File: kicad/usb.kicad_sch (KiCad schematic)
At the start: 4 parts, among them J7 USB_C_Receptacle_USB2.0_14P, U15 USBLC6-2SC6

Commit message: checking shunt footprints
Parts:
- renumbered J7 to J9, R37 to R45, R36 to R46
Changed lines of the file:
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@@
 		(on_board yes)
 		(dnp no)
-		(property "Reference" "R37"
+		(property "Reference" "R45"
 			(at 119.888 76.2 90)
 			(effects
@@
 			(project "resc"
 				(path "/83aea3b7-5b9b-498e-8d41-e84fae2f87fa/5f81bd15-f3fb-48c3-8997-18d2496b9ffc"
-					(reference "R37")
+					(reference "R45")
 					(unit 1)
 				)
@@
 		(dnp no)
 		(fields_autoplaced yes)
-		(property "Reference" "#PWR078"
+		(property "Reference" "#PWR089"
 			(at 92.71 120.65 0)
 			(effects
@@
 			(project "resc"
 				(path "/83aea3b7-5b9b-498e-8d41-e84fae2f87fa/5f81bd15-f3fb-48c3-8997-18d2496b9ffc"
-					(reference "#PWR078")
+					(reference "#PWR089")
 					(unit 1)
 				)
@@
 		(dnp no)
 		(fields_autoplaced yes)
-		(property "Reference" "#PWR082"
+		(property "Reference" "#PWR090"
 			(at 129.54 123.19 0)
 			(effects
@@
 			(project "resc"
 				(path "/83aea3b7-5b9b-498e-8d41-e84fae2f87fa/5f81bd15-f3fb-48c3-8997-18d2496b9ffc"
-					(reference "#PWR082")
+					(reference "#PWR090")
 					(unit 1)
 				)
@@
 		(on_board yes)
 		(dnp no)
-		(property "Reference" "#PWR080"
+		(property "Reference" "#PWR088"
 			(at 129.54 101.6 0)
 			(effects
@@
 			(project "resc"
 				(path "/83aea3b7-5b9b-498e-8d41-e84fae2f87fa/5f81bd15-f3fb-48c3-8997-18d2496b9ffc"
-					(reference "#PWR080")
+					(reference "#PWR088")
 					(unit 1)
 				)
@@
 		(dnp no)
 		(fields_autoplaced yes)
-		(property "Reference" "#PWR079"
+		(property "Reference" "#PWR086"
 			(at 114.3 73.66 0)
 			(effects
@@
 			(project ""
 				(path "/83aea3b7-5b9b-498e-8d41-e84fae2f87fa/5f81bd15-f3fb-48c3-8997-18d2496b9ffc"
-					(reference "#PWR079")
+					(reference "#PWR086")
 					(unit 1)
 				)
@@
 		(on_board yes)
 		(dnp no)
-		(property "Reference" "R36"
+		(property "Reference" "R46"
 			(at 119.634 81.28 90)
 			(effects
@@
 			(project "resc"
 				(path "/83aea3b7-5b9b-498e-8d41-e84fae2f87fa/5f81bd15-f3fb-48c3-8997-18d2496b9ffc"
-					(reference "R36")
+					(reference "R46")
 					(unit 1)
 				)
@@
 		(dnp no)
 		(fields_autoplaced yes)
-		(property "Reference" "J7"
+		(property "Reference" "J9"
 			(at 92.71 64.77 0)
 			(effects
@@
 			(project "resc"
 				(path "/83aea3b7-5b9b-498e-8d41-e84fae2f87fa/5f81bd15-f3fb-48c3-8997-18d2496b9ffc"
-					(reference "J7")
+					(reference "J9")
 					(unit 1)
 				)
@@
 		(on_board yes)
 		(dnp no)
-		(property "Reference" "#PWR081"
+		(property "Reference" "#PWR087"
 			(at 138.43 87.63 0)
 			(effects
@@
 			(project "resc"
 				(path "/83aea3b7-5b9b-498e-8d41-e84fae2f87fa/5f81bd15-f3fb-48c3-8997-18d2496b9ffc"
-					(reference "#PWR081")
-					(unit 1)
-				)
+					(reference "#PWR087")
+					(unit 1)
+				)

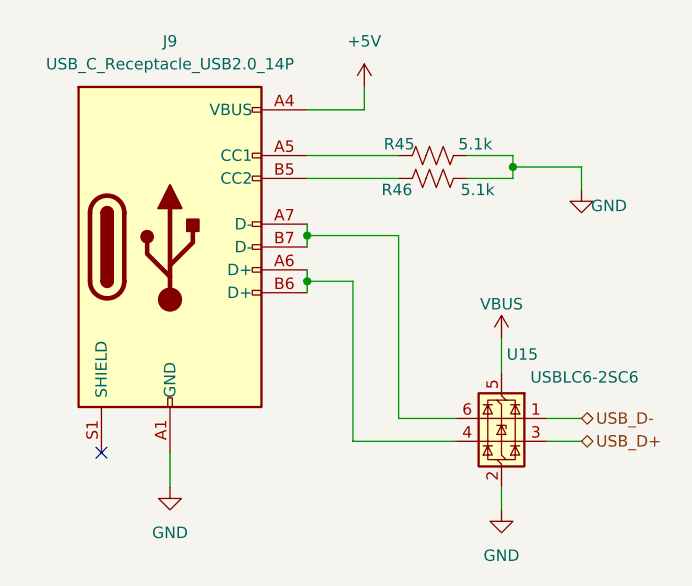
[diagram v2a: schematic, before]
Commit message: gate driver routed to mosfets, working on misc stm32 related components
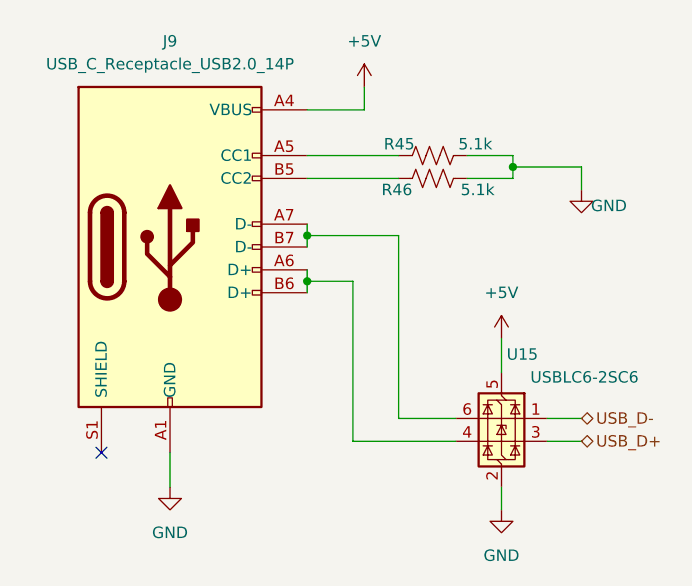
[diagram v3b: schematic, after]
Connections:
- net VBUS is gone; now on net +5V: U15.5 (VBUS)
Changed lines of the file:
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@@
 	)
 	(symbol
-		(lib_id "power:VBUS")
+		(lib_id "power:+5V")
 		(at 129.54 97.79 0)
 		(unit 1)
@@
 		(on_board yes)
 		(dnp no)
-		(property "Reference" "#PWR088"
+		(fields_autoplaced yes)
+		(property "Reference" "#PWR026"
 			(at 129.54 101.6 0)
 			(effects
@@
 			)
 		)
-		(property "Value" "VBUS"
-			(at 129.54 93.98 0)
+		(property "Value" "+5V"
+			(at 129.54 92.71 0)
 			(effects
 				(font
@@
 			)
 		)
-		(property "Description" "Power symbol creates a global label with name \"VBUS\""
+		(property "Description" "Power symbol creates a global label with name \"+5V\""
 			(at 129.54 97.79 0)
 			(effects
@@
 		)
 		(instances
-			(project "resc"
+			(project ""
 				(path "/83aea3b7-5b9b-498e-8d41-e84fae2f87fa/5f81bd15-f3fb-48c3-8997-18d2496b9ffc"
-					(reference "#PWR088")
+					(reference "#PWR026")
 					(unit 1)
 				)

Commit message: finalizing schematic for gate driver
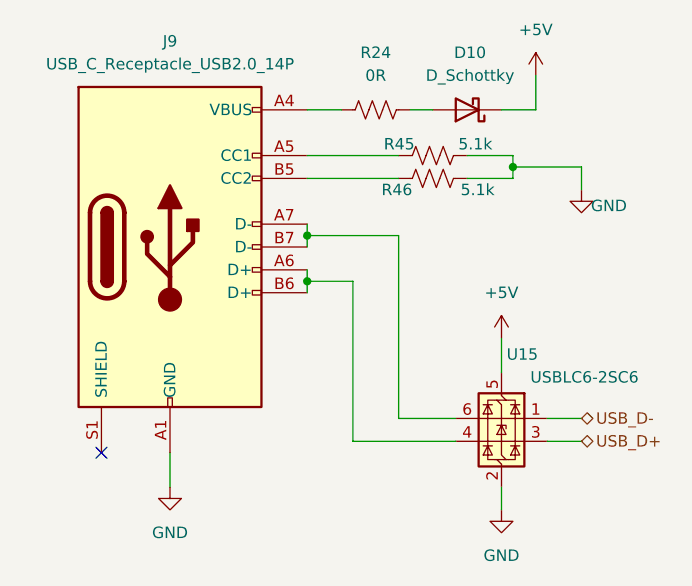
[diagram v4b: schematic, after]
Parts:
- added D10: D_Schottky, Diode_SMD:D_SOD-323_HandSoldering, symbol Device:D_Schottky
- added R24: 0R, Resistor_SMD:R_0402_1005Metric, symbol Device:R_US
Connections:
- net +5V: now also D10.1 (K); no longer J9.A4 (VBUS), J9.A9 (VBUS), J9.B4 (VBUS), J9.B9 (VBUS)
- new net: D10.2 (A), R24.2
- new net: J9.A4 (VBUS), J9.A9 (VBUS), J9.B4 (VBUS), J9.B9 (VBUS), R24.1
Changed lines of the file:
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@@
+	(wire
+		(pts
+			(xy 119.38 72.39) (xy 121.92 72.39)
+		)
+		(stroke
+			(width 0)
+			(type default)
+		)
+	)
 	(wire
 		(pts
@@
 	(wire
 		(pts
-			(xy 114.3 72.39) (xy 114.3 69.85)
+			(xy 133.35 72.39) (xy 133.35 68.58)
 		)
 		(stroke
@@
 	(wire
 		(pts
+			(xy 129.54 72.39) (xy 133.35 72.39)
+		)
+		(stroke
+			(width 0)
+			(type default)
+		)
+	)
+	(wire
+		(pts
 			(xy 129.54 114.3) (xy 129.54 116.84)
 		)
@@
 	(wire
 		(pts
+			(xy 107.95 72.39) (xy 111.76 72.39)
+		)
+		(stroke
+			(width 0)
+			(type default)
+		)
+	)
+	(wire
+		(pts
 			(xy 107.95 77.47) (xy 118.11 77.47)
-		)
-		(stroke
-			(width 0)
-			(type default)
-		)
-	)
-	(wire
-		(pts
-			(xy 107.95 72.39) (xy 114.3 72.39)
 		)
 		(stroke
@@
 	(symbol
 		(lib_id "power:+5V")
-		(at 114.3 69.85 0)
+		(at 133.35 68.58 0)
 		(unit 1)
 		(exclude_from_sim no)
@@
 		(fields_autoplaced yes)
 		(property "Reference" "#PWR086"
-			(at 114.3 73.66 0)
+			(at 133.35 72.39 0)
 			(effects
 				(font
@@
 		)
 		(property "Value" "+5V"
-			(at 114.3 64.77 0)
+			(at 133.35 63.5 0)
 			(effects
 				(font
@@
 		)
 		(property "Footprint" ""
-			(at 114.3 69.85 0)
+			(at 133.35 68.58 0)
 			(effects
 				(font
@@
 		)
 		(property "Datasheet" ""
-			(at 114.3 69.85 0)
+			(at 133.35 68.58 0)
 			(effects
 				(font
@@
 		)
 		(property "Description" "Power symbol creates a global label with name \"+5V\""
-			(at 114.3 69.85 0)
+			(at 133.35 68.58 0)
 			(effects
 				(font
@@
 				(path "/83aea3b7-5b9b-498e-8d41-e84fae2f87fa/5f81bd15-f3fb-48c3-8997-18d2496b9ffc"
 					(reference "#PWR086")
+					(unit 1)
+				)
+			)
+		)
+	)
+	(symbol
+		(lib_id "Device:D_Schottky")
+		(at 125.73 72.39 180)
+		(unit 1)
+		(exclude_from_sim no)
+		(in_bom yes)
+		(on_board yes)
+		(dnp no)
+		(fields_autoplaced yes)
+		(property "Reference" "D10"
+			(at 126.0475 66.04 0)
+			(effects
+				(font
+					(size 1.27 1.27)
+				)
+			)
+		)
+		(property "Value" "D_Schottky"
+			(at 126.0475 68.58 0)
+			(effects
+				(font
+					(size 1.27 1.27)
+				)
+			)
+		)
+		(property "Footprint" "Diode_SMD:D_SOD-323_HandSoldering"
+			(at 125.73 72.39 0)
+			(effects
+				(font
+					(size 1.27 1.27)
+				)
+				(hide yes)
+			)
+		)
+		(property "Datasheet" "~"
+			(at 125.73 72.39 0)
+			(effects
+				(font
+					(size 1.27 1.27)
+				)
+				(hide yes)
+			)
+		)
+		(property "Description" "Schottky diode"
+			(at 125.73 72.39 0)
+			(effects
+				(font
+					(size 1.27 1.27)
+				)
+				(hide yes)
+			)
+		)
+		(pin "1"
+		)
+		(pin "2"
+		)
+		(instances
+			(project ""
+				(path "/83aea3b7-5b9b-498e-8d41-e84fae2f87fa/5f81bd15-f3fb-48c3-8997-18d2496b9ffc"
+					(reference "D10")
 					(unit 1)
 				)
@@
 					(unit 1)
 				)
+			)
+		)
+	)
+	(symbol
+		(lib_id "Device:R_US")
+		(at 115.57 72.39 90)
+		(unit 1)
+		(exclude_from_sim no)
+		(in_bom yes)
+		(on_board yes)
+		(dnp no)
+		(fields_autoplaced yes)
+		(property "Reference" "R24"
+			(at 115.57 66.04 90)
+			(effects
+				(font
+					(size 1.27 1.27)
+				)
+			)
+		)
+		(property "Value" "0R"
+			(at 115.57 68.58 90)
+			(effects
+				(font
+					(size 1.27 1.27)
+				)
+			)
+		)
+		(property "Footprint" "Resistor_SMD:R_0402_1005Metric"
+			(at 115.824 71.374 90)
+			(effects
+				(font
+					(size 1.27 1.27)
+				)
+				(hide yes)
+			)
+		)
+		(property "Datasheet" "~"
+			(at 115.57 72.39 0)
+			(effects
+				(font
+					(size 1.27 1.27)
+				)
+				(hide yes)
+			)
+		)
+		(property "Description" "Resistor, US symbol"
+			(at 115.57 72.39 0)
+			(effects
+				(font
+					(size 1.27 1.27)
+				)
+				(hide yes)
+			)
+		)
+		(pin "2"
+		)
+		(pin "1"
+		)
+		(instances
+			(project ""
+				(path "/83aea3b7-5b9b-498e-8d41-e84fae2f87fa/5f81bd15-f3fb-48c3-8997-18d2496b9ffc"
+					(reference "R24")
+					(unit 1)
+				)

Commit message: revert to v6.05
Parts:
- removed R24: 0R, Resistor_SMD:R_0402_1005Metric, symbol Device:R_US
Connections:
- net at D10.2 (A): now also J9.A4 (VBUS), J9.A9 (VBUS), J9.B4 (VBUS), J9.B9 (VBUS)
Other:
- moved on the sheet: D10
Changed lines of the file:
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@@
-	(wire
-		(pts
-			(xy 119.38 72.39) (xy 121.92 72.39)
-		)
-		(stroke
-			(width 0)
-			(type default)
-		)
-	)
 	(wire
 		(pts
@@
 	(wire
 		(pts
+			(xy 123.19 72.39) (xy 133.35 72.39)
+		)
+		(stroke
+			(width 0)
+			(type default)
+		)
+	)
+	(wire
+		(pts
 			(xy 133.35 72.39) (xy 133.35 68.58)
 		)
@@
 	(wire
 		(pts
-			(xy 129.54 72.39) (xy 133.35 72.39)
-		)
-		(stroke
-			(width 0)
-			(type default)
-		)
-	)
-	(wire
-		(pts
 			(xy 129.54 114.3) (xy 129.54 116.84)
 		)
@@
 	(wire
 		(pts
+			(xy 107.95 72.39) (xy 115.57 72.39)
+		)
+		(stroke
+			(width 0)
+			(type default)
+		)
+	)
+	(wire
+		(pts
 			(xy 92.71 110.49) (xy 92.71 114.3)
 		)
@@
 		(pts
 			(xy 107.95 86.36) (xy 107.95 87.63)
-		)
-		(stroke
-			(width 0)
-			(type default)
-		)
-	)
-	(wire
-		(pts
-			(xy 107.95 72.39) (xy 111.76 72.39)
 		)
 		(stroke
@@
 	(symbol
 		(lib_id "Device:D_Schottky")
-		(at 125.73 72.39 180)
+		(at 119.38 72.39 180)
 		(unit 1)
 		(exclude_from_sim no)
@@
 		(fields_autoplaced yes)
 		(property "Reference" "D10"
-			(at 126.0475 66.04 0)
+			(at 119.6975 66.04 0)
 			(effects
 				(font
@@
 		)
 		(property "Value" "D_Schottky"
-			(at 126.0475 68.58 0)
+			(at 119.6975 68.58 0)
 			(effects
 				(font
@@
 		)
 		(property "Footprint" "Diode_SMD:D_SOD-323_HandSoldering"
-			(at 125.73 72.39 0)
+			(at 119.38 72.39 0)
 			(effects
 				(font
@@
 		)
 		(property "Datasheet" "~"
-			(at 125.73 72.39 0)
+			(at 119.38 72.39 0)
 			(effects
 				(font
@@
 		)
 		(property "Description" "Schottky diode"
-			(at 125.73 72.39 0)
+			(at 119.38 72.39 0)
 			(effects
 				(font
@@
 					(unit 1)
 				)
-			)
-		)
-	)
-	(symbol
-		(lib_id "Device:R_US")
-		(at 115.57 72.39 90)
-		(unit 1)
-		(exclude_from_sim no)
-		(in_bom yes)
-		(on_board yes)
-		(dnp no)
-		(fields_autoplaced yes)
-		(property "Reference" "R24"
-			(at 115.57 66.04 90)
-			(effects
-				(font
-					(size 1.27 1.27)
-				)
-			)
-		)
-		(property "Value" "0R"
-			(at 115.57 68.58 90)
-			(effects
-				(font
-					(size 1.27 1.27)
-				)
-			)
-		)
-		(property "Footprint" "Resistor_SMD:R_0402_1005Metric"
-			(at 115.824 71.374 90)
-			(effects
-				(font
-					(size 1.27 1.27)
-				)
-				(hide yes)
-			)
-		)
-		(property "Datasheet" "~"
-			(at 115.57 72.39 0)
-			(effects
-				(font
-					(size 1.27 1.27)
-				)
-				(hide yes)
-			)
-		)
-		(property "Description" "Resistor, US symbol"
-			(at 115.57 72.39 0)
-			(effects
-				(font
-					(size 1.27 1.27)
-				)
-				(hide yes)
-			)
-		)
-		(pin "2"
-		)
-		(pin "1"
-		)
-		(instances
-			(project ""
-				(path "/83aea3b7-5b9b-498e-8d41-e84fae2f87fa/5f81bd15-f3fb-48c3-8997-18d2496b9ffc"
-					(reference "R24")
-					(unit 1)
-				)

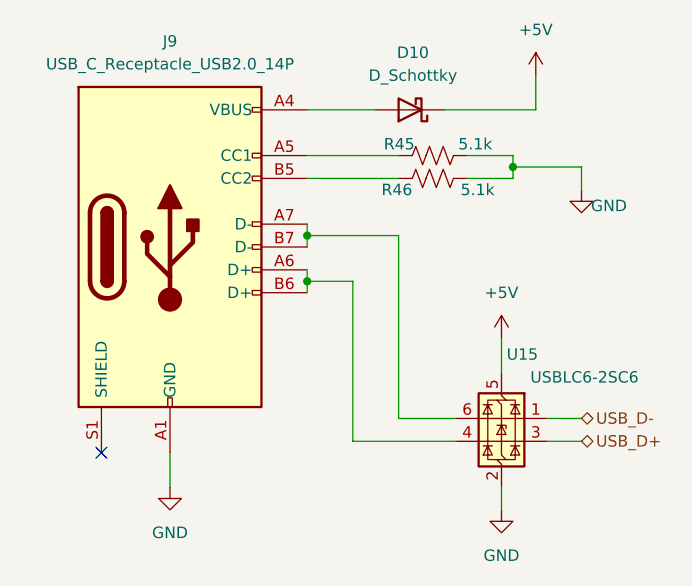
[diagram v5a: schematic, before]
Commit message: gate driver mostly schematic'd and pcb started
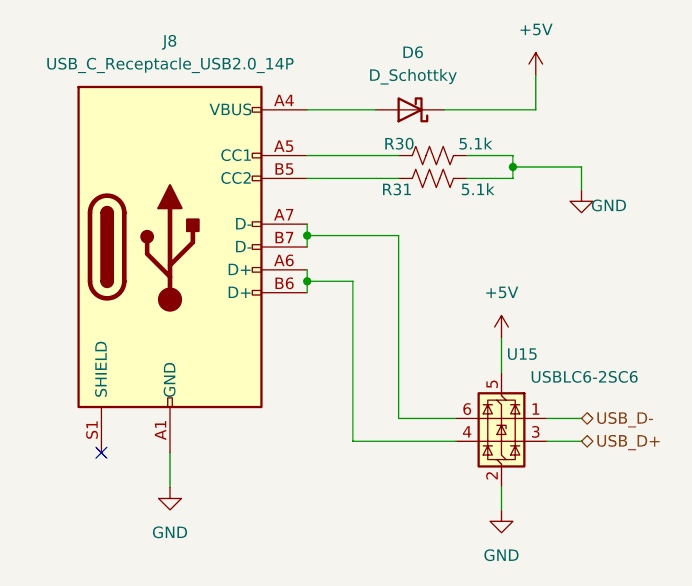
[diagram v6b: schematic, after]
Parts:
- renumbered D10 to D6, J9 to J8, R45 to R30, R46 to R31
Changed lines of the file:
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@@
 		(on_board yes)
 		(dnp no)
-		(property "Reference" "R45"
+		(property "Reference" "R30"
 			(at 119.888 76.2 90)
 			(effects
@@
 			(project "resc"
 				(path "/83aea3b7-5b9b-498e-8d41-e84fae2f87fa/5f81bd15-f3fb-48c3-8997-18d2496b9ffc"
-					(reference "R45")
+					(reference "R30")
 					(unit 1)
 				)
@@
 		(dnp no)
 		(fields_autoplaced yes)
-		(property "Reference" "#PWR089"
+		(property "Reference" "#PWR076"
 			(at 92.71 120.65 0)
 			(effects
@@
 			(project "resc"
 				(path "/83aea3b7-5b9b-498e-8d41-e84fae2f87fa/5f81bd15-f3fb-48c3-8997-18d2496b9ffc"
-					(reference "#PWR089")
+					(reference "#PWR076")
 					(unit 1)
 				)
@@
 		(dnp no)
 		(fields_autoplaced yes)
-		(property "Reference" "#PWR090"
+		(property "Reference" "#PWR077"
 			(at 129.54 123.19 0)
 			(effects
@@
 			(project "resc"
 				(path "/83aea3b7-5b9b-498e-8d41-e84fae2f87fa/5f81bd15-f3fb-48c3-8997-18d2496b9ffc"
-					(reference "#PWR090")
+					(reference "#PWR077")
 					(unit 1)
 				)
@@
 		(dnp no)
 		(fields_autoplaced yes)
-		(property "Reference" "#PWR026"
+		(property "Reference" "#PWR075"
 			(at 129.54 101.6 0)
 			(effects
@@
 			(project ""
 				(path "/83aea3b7-5b9b-498e-8d41-e84fae2f87fa/5f81bd15-f3fb-48c3-8997-18d2496b9ffc"
-					(reference "#PWR026")
+					(reference "#PWR075")
 					(unit 1)
 				)
@@
 		(dnp no)
 		(fields_autoplaced yes)
-		(property "Reference" "#PWR086"
+		(property "Reference" "#PWR073"
 			(at 133.35 72.39 0)
 			(effects
@@
 			(project ""
 				(path "/83aea3b7-5b9b-498e-8d41-e84fae2f87fa/5f81bd15-f3fb-48c3-8997-18d2496b9ffc"
-					(reference "#PWR086")
+					(reference "#PWR073")
 					(unit 1)
 				)
@@
 		(dnp no)
 		(fields_autoplaced yes)
-		(property "Reference" "D10"
+		(property "Reference" "D6"
 			(at 119.6975 66.04 0)
 			(effects
@@
 			(project ""
 				(path "/83aea3b7-5b9b-498e-8d41-e84fae2f87fa/5f81bd15-f3fb-48c3-8997-18d2496b9ffc"
-					(reference "D10")
+					(reference "D6")
 					(unit 1)
 				)
@@
 		(on_board yes)
 		(dnp no)
-		(property "Reference" "R46"
+		(property "Reference" "R31"
 			(at 119.634 81.28 90)
 			(effects
@@
 			(project "resc"
 				(path "/83aea3b7-5b9b-498e-8d41-e84fae2f87fa/5f81bd15-f3fb-48c3-8997-18d2496b9ffc"
-					(reference "R46")
+					(reference "R31")
 					(unit 1)
 				)
@@
 		(dnp no)
 		(fields_autoplaced yes)
-		(property "Reference" "J9"
+		(property "Reference" "J8"
 			(at 92.71 64.77 0)
 			(effects
@@
 			(project "resc"
 				(path "/83aea3b7-5b9b-498e-8d41-e84fae2f87fa/5f81bd15-f3fb-48c3-8997-18d2496b9ffc"
-					(reference "J9")
+					(reference "J8")
 					(unit 1)
 				)
@@
 		(on_board yes)
 		(dnp no)
-		(property "Reference" "#PWR087"
+		(property "Reference" "#PWR074"
 			(at 138.43 87.63 0)
 			(effects
@@
 			(project "resc"
 				(path "/83aea3b7-5b9b-498e-8d41-e84fae2f87fa/5f81bd15-f3fb-48c3-8997-18d2496b9ffc"
-					(reference "#PWR087")
-					(unit 1)
-				)
+					(reference "#PWR074")
+					(unit 1)
+				)

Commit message: rev3 ordered
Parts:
- renumbered D6 to D10, J8 to J9, R30 to R45, R31 to R46
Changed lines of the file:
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@@
 		(on_board yes)
 		(dnp no)
-		(property "Reference" "R30"
+		(property "Reference" "R45"
 			(at 119.888 76.2 90)
 			(effects
@@
 			(project "resc"
 				(path "/83aea3b7-5b9b-498e-8d41-e84fae2f87fa/5f81bd15-f3fb-48c3-8997-18d2496b9ffc"
-					(reference "R30")
+					(reference "R45")
 					(unit 1)
 				)
@@
 		(dnp no)
 		(fields_autoplaced yes)
-		(property "Reference" "#PWR076"
+		(property "Reference" "#PWR089"
 			(at 92.71 120.65 0)
 			(effects
@@
 			(project "resc"
 				(path "/83aea3b7-5b9b-498e-8d41-e84fae2f87fa/5f81bd15-f3fb-48c3-8997-18d2496b9ffc"
-					(reference "#PWR076")
+					(reference "#PWR089")
 					(unit 1)
 				)
@@
 		(dnp no)
 		(fields_autoplaced yes)
-		(property "Reference" "#PWR077"
+		(property "Reference" "#PWR090"
 			(at 129.54 123.19 0)
 			(effects
@@
 			(project "resc"
 				(path "/83aea3b7-5b9b-498e-8d41-e84fae2f87fa/5f81bd15-f3fb-48c3-8997-18d2496b9ffc"
-					(reference "#PWR077")
+					(reference "#PWR090")
 					(unit 1)
 				)
@@
 		(dnp no)
 		(fields_autoplaced yes)
-		(property "Reference" "#PWR075"
+		(property "Reference" "#PWR026"
 			(at 129.54 101.6 0)
 			(effects
@@
 			(project ""
 				(path "/83aea3b7-5b9b-498e-8d41-e84fae2f87fa/5f81bd15-f3fb-48c3-8997-18d2496b9ffc"
-					(reference "#PWR075")
+					(reference "#PWR026")
 					(unit 1)
 				)
@@
 		(dnp no)
 		(fields_autoplaced yes)
-		(property "Reference" "#PWR073"
+		(property "Reference" "#PWR086"
 			(at 133.35 72.39 0)
 			(effects
@@
 			(project ""
 				(path "/83aea3b7-5b9b-498e-8d41-e84fae2f87fa/5f81bd15-f3fb-48c3-8997-18d2496b9ffc"
-					(reference "#PWR073")
+					(reference "#PWR086")
 					(unit 1)
 				)
@@
 		(dnp no)
 		(fields_autoplaced yes)
-		(property "Reference" "D6"
+		(property "Reference" "D10"
 			(at 119.6975 66.04 0)
 			(effects
@@
 			(project ""
 				(path "/83aea3b7-5b9b-498e-8d41-e84fae2f87fa/5f81bd15-f3fb-48c3-8997-18d2496b9ffc"
-					(reference "D6")
+					(reference "D10")
 					(unit 1)
 				)
@@
 		(on_board yes)
 		(dnp no)
-		(property "Reference" "R31"
+		(property "Reference" "R46"
 			(at 119.634 81.28 90)
 			(effects
@@
 			(project "resc"
 				(path "/83aea3b7-5b9b-498e-8d41-e84fae2f87fa/5f81bd15-f3fb-48c3-8997-18d2496b9ffc"
-					(reference "R31")
+					(reference "R46")
 					(unit 1)
 				)
@@
 		(dnp no)
 		(fields_autoplaced yes)
-		(property "Reference" "J8"
+		(property "Reference" "J9"
 			(at 92.71 64.77 0)
 			(effects
@@
 			(project "resc"
 				(path "/83aea3b7-5b9b-498e-8d41-e84fae2f87fa/5f81bd15-f3fb-48c3-8997-18d2496b9ffc"
-					(reference "J8")
+					(reference "J9")
 					(unit 1)
 				)
@@
 		(on_board yes)
 		(dnp no)
-		(property "Reference" "#PWR074"
+		(property "Reference" "#PWR087"
 			(at 138.43 87.63 0)
 			(effects
@@
 			(project "resc"
 				(path "/83aea3b7-5b9b-498e-8d41-e84fae2f87fa/5f81bd15-f3fb-48c3-8997-18d2496b9ffc"
-					(reference "#PWR074")
-					(unit 1)
-				)
+					(reference "#PWR087")
+					(unit 1)
+				)
